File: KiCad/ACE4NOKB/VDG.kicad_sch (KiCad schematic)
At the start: 39 parts, among them Q1 2N3904, Q100 2N3904, X1 CRYSTALHC49U-V 6.5MHz

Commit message: Fix mistake with ROM Select.
Signed-off-by: John Bradley <flypie@rocketmail.com>
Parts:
- removed C1: 30p, Capacitor_THT:C_Disc_D3.8mm_W2.6mm_P2.50mm, symbol Device:C_Small
- removed C2: 100p, Capacitor_THT:C_Disc_D5.0mm_W2.5mm_P5.00mm, symbol Device:C_Small
- removed D100: BAT54W,115, Package_TO_SOT_SMD:SOT-323_SC-70, symbol Diode:BAT54W
- removed D11: 1N4148, Diode_THT:D_DO-35_SOD27_P2.54mm_Vertical_AnodeUp, symbol Diode:1N4148
- removed IC? (x2): 74ACT16825DL, SOP64P1035X279-56N, symbol ExtraSymbols:74ACT16825DL
- removed JCOMPOSITE-OUT1: COMPOSITE-OUT1, Connector_PinHeader_2.54mm:PinHeader_1x02_P2.54mm_Vertical, symbol Connector_Generic:Conn_01x02
- removed Q1, Q100: 2N3904, Package_TO_SOT_THT:TO-92_Inline, symbol Transistor_BJT:2N3904
- removed R1: 4k7, Resistor_THT:R_Axial_DIN0204_L3.6mm_D1.6mm_P1.90mm_Vertical, symbol Device:R
- removed R11, R16: 1K5, Resistor_THT:R_Axial_DIN0204_L3.6mm_D1.6mm_P1.90mm_Vertical, symbol Device:R
- removed R17: 100, Resistor_THT:R_Axial_DIN0204_L3.6mm_D1.6mm_P1.90mm_Vertical, symbol Device:R
- removed R2: 47k, Resistor_THT:R_Axial_DIN0204_L3.6mm_D1.6mm_P1.90mm_Vertical, symbol Device:R
- removed R404, R406, R407: 270, Resistor_THT:R_Axial_DIN0204_L3.6mm_D1.6mm_P1.90mm_Vertical, symbol Device:R
- removed R416, R417: 75k, Resistor_THT:R_Axial_DIN0204_L3.6mm_D1.6mm_P1.90mm_Vertical, symbol Device:R
- removed R418, R419, R420, R422, R? (x2): 1k0, Resistor_THT:R_Axial_DIN0204_L3.6mm_D1.6mm_P1.90mm_Vertical, symbol Device:R
- removed R421: 10k, Resistor_THT:R_Axial_DIN0204_L3.6mm_D1.6mm_P1.90mm_Vertical, symbol Device:R
- removed RV1: 100, ExtraFootprints:3362H1103LF, symbol Device:R_Potentiometer_Trim
- removed X1: CRYSTALHC49U-V 6.5MHz, Crystal:Crystal_HC49-U_Vertical, symbol Device:Crystal
- removed Z19: 74AHCT00, Package_DIP:DIP-14_W7.62mm_Socket, symbol 74xx:74HCT00
- removed Z23: 74AHCT1G86GW,125, ExtraFootprints:TSSOP-5, symbol ExtraSymbols:74AHC1G86GW,125
- removed Z25: 74AHCT02, Package_DIP:DIP-14_W7.62mm_Socket, symbol 74xx:74HCT02
- removed Z28: 74HCT166, Package_DIP:DIP-16_W7.62mm_Socket, symbol 74xx:74LS166
- removed Z306: 74AHCT04, Package_DIP:DIP-14_W7.62mm_Socket, symbol 74xx:74LS04
- removed Z7-8: IDT71321, ExtraFootprints:PLCC-52, symbol ExtraSymbols:IDT71321-421-52PIN-PLCC
- added COMP1: PJRAN1X1U03, ExtraFootprints:PJRAN1X1U01X, symbol ExtraSymbols:PJRAN1X1U03AUX
- added D1: 1N4148, Diode_THT:D_DO-35_SOD27_P2.54mm_Vertical_AnodeUp, symbol Diode:1N4148
- added Q101: 2N3904, Package_TO_SOT_THT:TO-92_Inline, symbol Transistor_BJT:2N3904
- added R100: 100, Resistor_THT:R_Axial_DIN0204_L3.6mm_D1.6mm_P1.90mm_Vertical, symbol Device:R
- added R134, R135, R21, R22, R400, R401, R402: 1K, Resistor_THT:R_Axial_DIN0204_L3.6mm_D1.6mm_P1.90mm_Vertical, symbol Device:R
- added R136, R403: 10K, Resistor_THT:R_Axial_DIN0204_L3.6mm_D1.6mm_P1.90mm_Vertical, symbol Device:R
- added R3, R4: 1K5, Resistor_THT:R_Axial_DIN0204_L3.6mm_D1.6mm_P1.90mm_Vertical, symbol Device:R
- added RN2, RN3: 1k, Package_DIP:DIP-16_W7.62mm, symbol Device:R_Pack08
- added RV101: 100, Potentiometer_THT:Potentiometer_Bourns_3296W_Vertical, symbol Device:R_Potentiometer_Trim
- added Z18: 74LS125, Package_DIP:DIP-14_W7.62mm, symbol 74xx-FIX:74LS125
- added Z19: SN74AHCT00N, Package_DIP:DIP-14_W7.62mm, symbol 74xx:74LS00
- added unit 1 of Z20
- added Z21: SN74ACT11N, Package_DIP:DIP-14_W7.62mm, symbol 74xx:74LS11
- added Z23: SN74AHCT86N, Package_DIP:DIP-14_W7.62mm, symbol 74xx:74LS86
- added Z25: SN74AHCT02, Package_DIP:DIP-14_W7.62mm, symbol 74xx:74LS02
- added Z28: SN74ALS166N, Package_DIP:DIP-16_W7.62mm, symbol 74xx-FIX:74LS166
- added Z7-8: 6116P, Package_DIP:DIP-24_W7.62mm, symbol ExtraSymbols:6116P
- R405: value 270 -> 1K; Manufacturer_Part_Number CCF07270RGKE36 -> MBA02040C4708FRP00
- Z20: value 74AHCT08 -> SN74AHCT08N; footprint Package_DIP:DIP-14_W7.62mm_Socket -> Package_DIP:DIP-14_W7.62mm; Manufacturer_Name Texas Instruments -> (none); Manufacturer_Part_Number SN74AHCT08N -> (none)
- Z22: value 74HCT11 -> SN74ACT11N; footprint Package_DIP:DIP-14_W7.62mm_Socket -> Package_DIP:DIP-14_W7.62mm; Manufacturer_Name Texas Instruments -> (none); Manufacturer_Part_Number CD74HCT11M -> (none)
- Z27: value 74AHCT74 -> SN74AHCT74N; footprint Package_DIP:DIP-14_W7.62mm_Socket -> Package_DIP:DIP-14_W7.62mm; Manufacturer_Name Texas Instruments -> (none); Manufacturer_Part_Number SN74AHCT74N -> (none)
- Z5-6: value IDT71321 -> 7132LA100PDG; footprint ExtraFootprints:PLCC-52 -> ExtraFootprints:PLCC-52_THT-Socket
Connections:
- net A0: now also RN3.1 (R1.1)
- net A1: now also RN3.2 (R2.1)
- net A2: now also RN3.3 (R3.1)
- net A3: now also RN3.4 (R4.1)
- net A4: now also RN3.5 (R5.1)
- net A5: now also RN3.6 (R6.1)
- net A6: now also RN3.7 (R7.1)
- net A7: now also RN3.8 (R8.1)
- net A8: now also R21.1
- net A9: now also R22.1
- net GND: now also R405.1, COMP1.1 (SLEEVE), R100.2, R134.1, R135.1, R400.1, R401.1, R402.1, Z28.8 (GND), Z7-8.12 (GND)
- net SCREENX2: now also Z21.9, Z25.8
- net SCREENX4: now also Z21.10, Z25.9
- net SCREENY0: now also Z21.1
- net SCREENY1: now also Z21.2
- net SCREENY2: now also Z21.13
- net SCREENY3: now also Z19.2, Z21.3
- net SCREENY4: now also Z19.1, Z21.4
- net VCC: now also Q101.3 (C), R136.1, R4.1, R403.1, Z28.16 (VCC), Z7-8.24 (VCC); no longer R405.2
- net VIDEO: now also Q101.1 (E), R100.1, RV101.1
- net at Z27.9 (Q): now also Z23.12
- net at Z20.4: now also Z19.3
- net ~{IN_VBI_OR_HBI}: now reaches Z20.12, Z20.6
- net ~{IN_VBI_OR_HBI}: now also Z19.4
- net at Z20.5: now also Z25.1
- net VA9: now reaches Z5-6.33 (I/O6_{R})
- net VA9: now also R22.2, Z7-8.22 (A9)
- net VA8: now reaches Z5-6.32 (I/O5_{R})
- net VA8: now also R21.2, Z7-8.23 (A8)
- net VA7: now reaches Z5-6.31 (I/O4_{R})
- net VA7: now also RN3.9 (R8.2), Z7-8.1 (A7)
- net VA6: now reaches Z5-6.30 (I/O3_{R})
- net VA6: now also RN3.10 (R7.2), Z7-8.2 (A6)
- net VA5: now reaches Z5-6.29 (I/O2_{R})
- net VA5: now also RN3.11 (R6.2), Z7-8.3 (A5)
- net VA4: now reaches Z5-6.28 (I/O1_{R})
- net VA4: now also RN3.12 (R5.2), Z7-8.4 (A4)
- net VA3: now reaches Z5-6.27 (I/O0_{R})
- net VA3: now also RN3.13 (R4.2), Z7-8.5 (A3)
- net at Z5-6.3 (~{BUSY}_{L}): no longer R405.1
- net at Z5-6.47 (A10_{R}): now also R401.2
- net at Z5-6.5 (A10_{L}): now also R400.2
- net at Z5-6.50 (R/~{W}_{R}): now also R403.2
- net H_SYNC_PULSE: now reaches Z22.12
- net H_SYNC_PULSE: now also Z25.5
- net at Z22.2: now also Z25.10
- net CNT0 renamed FONTCHARX0
- net CNT1 renamed FONTCHARX1
- net CNT2 renamed FONTCHARX2
- net DA0 renamed D0
- net D0: now also RN2.1 (R1.1)
- net DA1 renamed D1
- net D1: now also RN2.2 (R2.1)
- net DA2 renamed D2
- net D2: now also RN2.3 (R3.1)
- net DA3 renamed D3
- net D3: now also RN2.4 (R4.1)
- net DA4 renamed D4
- net D4: now also RN2.5 (R5.1)
- net DA5 renamed D5
- net D5: now also RN2.6 (R6.1)
- net DA6 renamed D6
- net D6: now also RN2.7 (R7.1)
- net DA7 renamed D7
- net D7: now also RN2.8 (R8.1)
- net EOL renamed SCREENX5
- net SCREENX5: now also Z21.11, Z25.3
- net SH~{LD}: no longer names the net of Z5-6.51 (~{CE}_{R})
- net SH~{LD}: now also R402.2; no longer Z5-6.46 (~{OER})
- net VIDEN renamed LOAD_SHIFT_REG
- net LOAD_SHIFT_REG: now also Z19.5
- net ~{CPUVIDEORAM} renamed ~{CPU2VRAM}
- net ~{VIDEOCLK} renamed VDGCLK
- net VDGCLK: now also Z28.7 (CLK)
- net ~{WAIT}: no longer names the net of Z5-6.49 (~{BUSY}_{R})
- new net: R134.2, Z28.1 (SER)
- new net: R135.2, Z28.6 (CLK_INH)
- new net: R136.2, Z28.9 (~{CLR})
- new net: R3.2, Z23.11
- new net: Z20.1, Z21.12, Z21.5
- new net: R405.2, Z7-8.19 (A10)
- new net: COMP1.2 (TIP), RV101.2
- new net FONTCHARY0: Z18.5
- new net FONTCHARY1: Z18.9
- new net FONTCHARY2: Z18.12
- new net PIXEL: Z23.13, Z28.13 (Qh)
- new net RAWVIDEO: D1.2 (A), Q101.2 (B), R3.1, R4.2
- new net SCREENY5: Z20.2, Z25.2
- new net SHIFT/~{LOAD}: Z19.6, Z28.15 (SH/~{LD}), Z5-6.46 (~{OE}_{R})
- new net VA0: RN3.16 (R1.2), Z18.6, Z7-8.8 (A0)
- new net VA1: RN3.15 (R2.2), Z18.8, Z7-8.7 (A1)
- new net VA2: RN3.14 (R3.2), Z18.11, Z7-8.6 (A2)
- new net VD0: RN2.16 (R1.2), Z28.2 (A), Z7-8.9 (D0)
- new net VD1: RN2.15 (R2.2), Z28.3 (B), Z7-8.10 (D1)
- new net VD2: RN2.14 (R3.2), Z28.4 (C), Z7-8.11 (D2)
- new net VD3: RN2.13 (R4.2), Z28.5 (D), Z7-8.13 (D3)
- new net VD4: RN2.12 (R5.2), Z28.10 (E), Z7-8.14 (D4)
- new net VD5: RN2.11 (R6.2), Z28.11 (F), Z7-8.15 (D5)
- new net VD6: RN2.10 (R7.2), Z28.12 (G), Z7-8.16 (D6)
- new net VD7: RN2.9 (R8.2), Z28.14 (H), Z7-8.17 (D7)
- new net V_SYNC_PULSE(50Hz): Z21.6, Z25.6
- new net XRESET: Z21.8
- new net YRESET: Z20.3
- new net ~{CPUVDGRD}: Z18.10, Z18.13, Z18.4, Z7-8.20 (~{OE})
- new net ~{CPUVDGWR}: Z7-8.21 (~{WE})
- new net ~{FONTRAMCS}: Z7-8.18 (~{CS})
- new net ~{SYNC_PULSE}: D1.1 (K), Z25.4
- no-connect marks 6 -> 7
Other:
- removed sheet Cascade4040
- note added: "END_OF_PIX_V"
- title: ACE4NOKB -> JupiterAce Z80 plus KIO and new memory format.

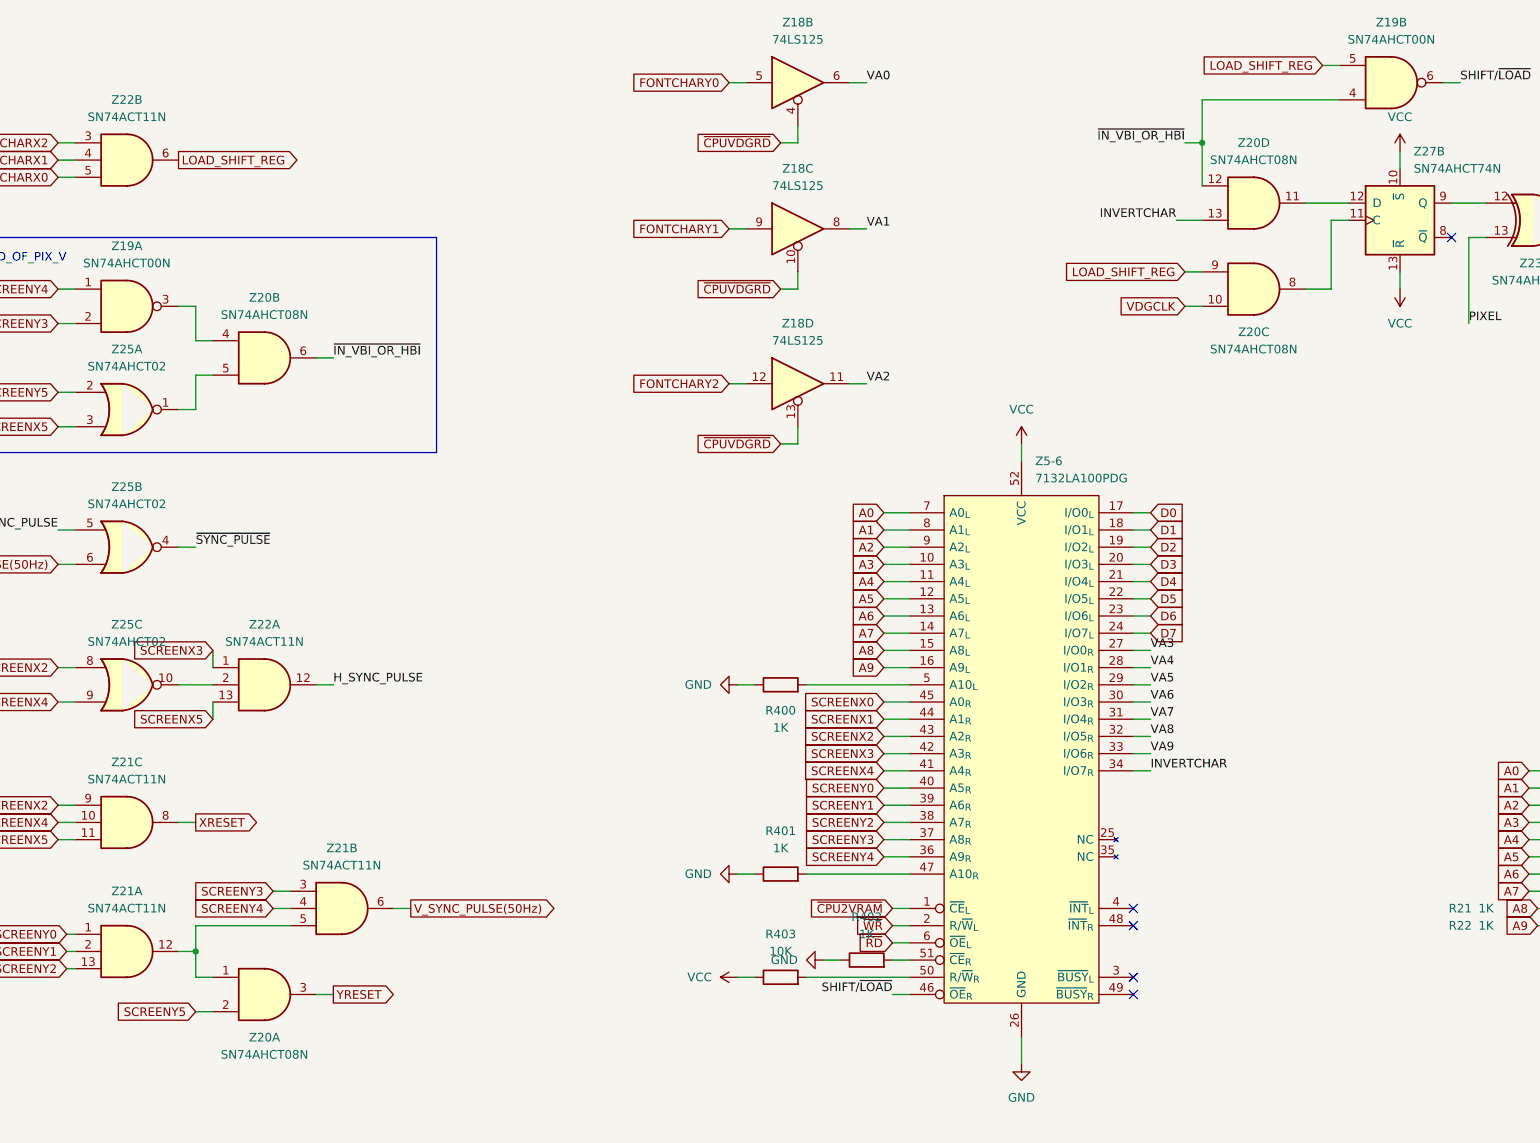
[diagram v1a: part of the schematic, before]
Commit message: Update to last expermintal version. Uses clock sythsiser and can be switched between full ACE compatible and inhanced IO. Should be able to switch between multiple ROM images tosred on the same chip.
Signed-off-by: John Bradley <flypie@rocketmail.com>
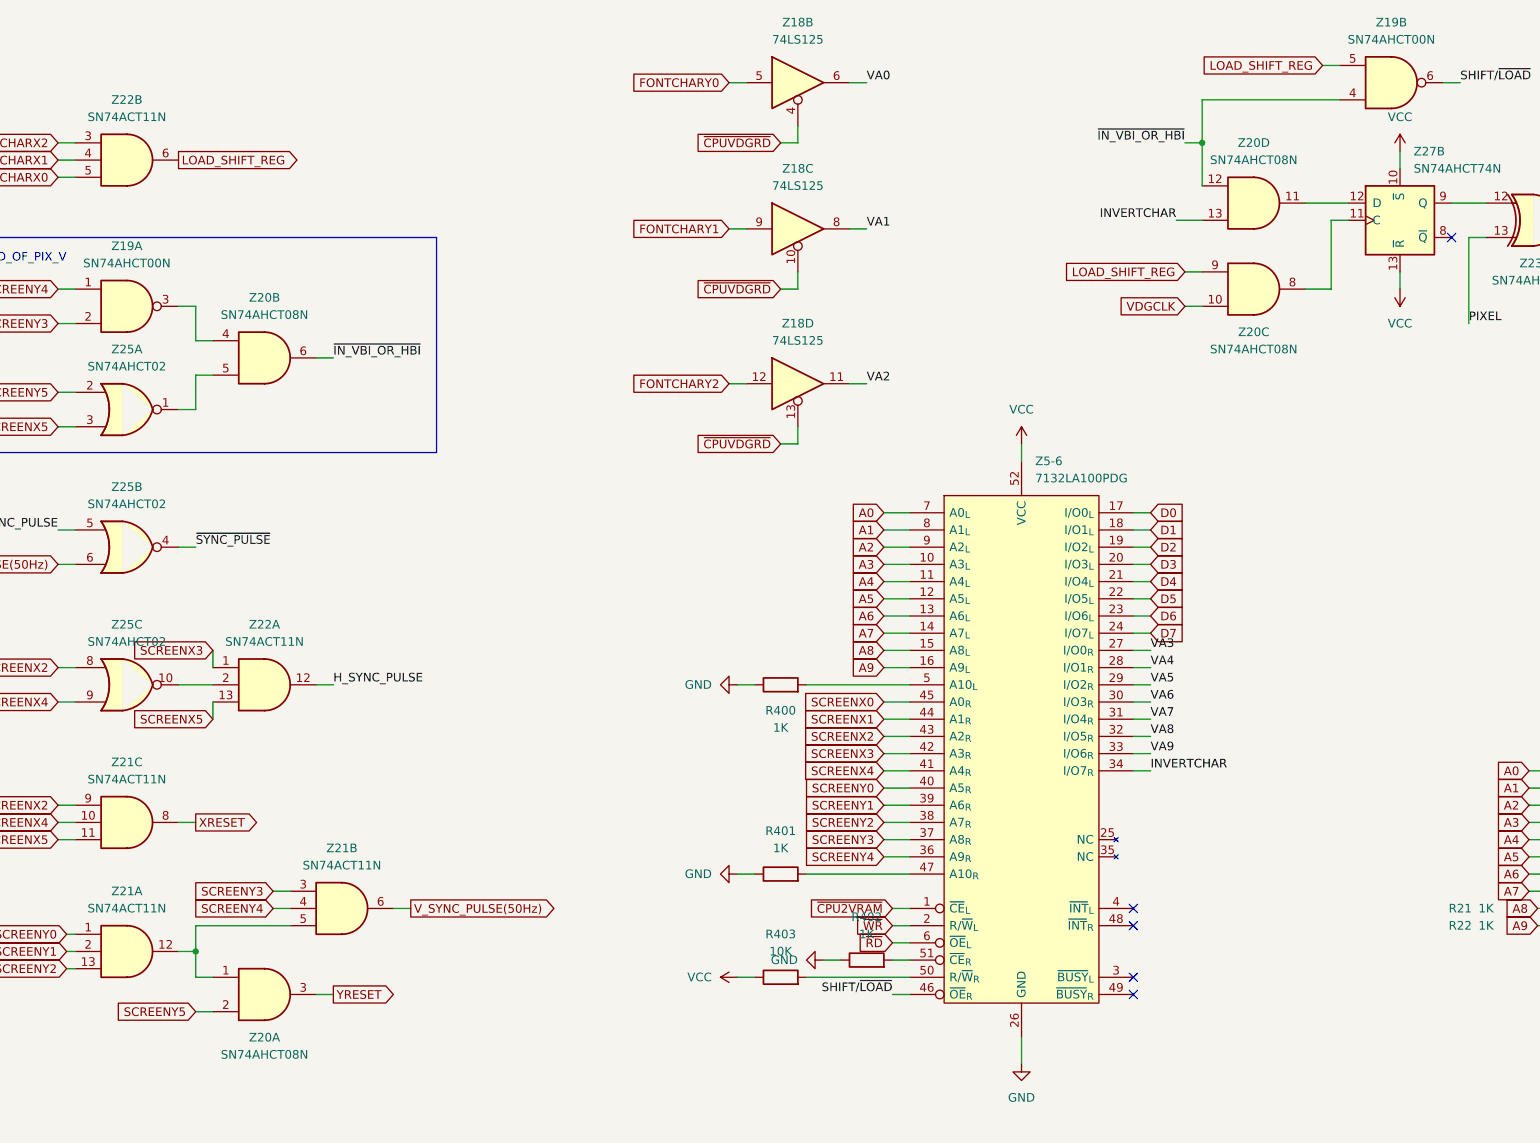
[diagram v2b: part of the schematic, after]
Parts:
- COMP1: Field4 (none) -> Conn Rca Jack Mono 3.2mm r/a; Field5 (none) -> None; Field6 (none) -> PJRAN1X1U03AUX; Field7 (none) -> Unavailable; Field8 (none) -> Switchcraft Inc.
- R134, R135: Manufacturer_Name Vishay -> (none); Manufacturer_Part_Number MBA02040C1202FRP00 -> (none)
- R136: Manufacturer_Name Vishay -> (none); Manufacturer_Part_Number MBA02040C1002FRP00 -> (none)
- R400, R401, R402, R403, R405: Manufacturer_Name Vishay -> (none); Manufacturer_Part_Number MBA02040C4708FRP00 -> (none)
- Z25: Manufacturer_Name Texas Instruments -> (none); Manufacturer_Part_Number SN74AHCT02N -> (none)
- Z28: Manufacturer_Name Texas Instruments -> (none); Manufacturer_Part_Number SN74ALS166N -> (none)

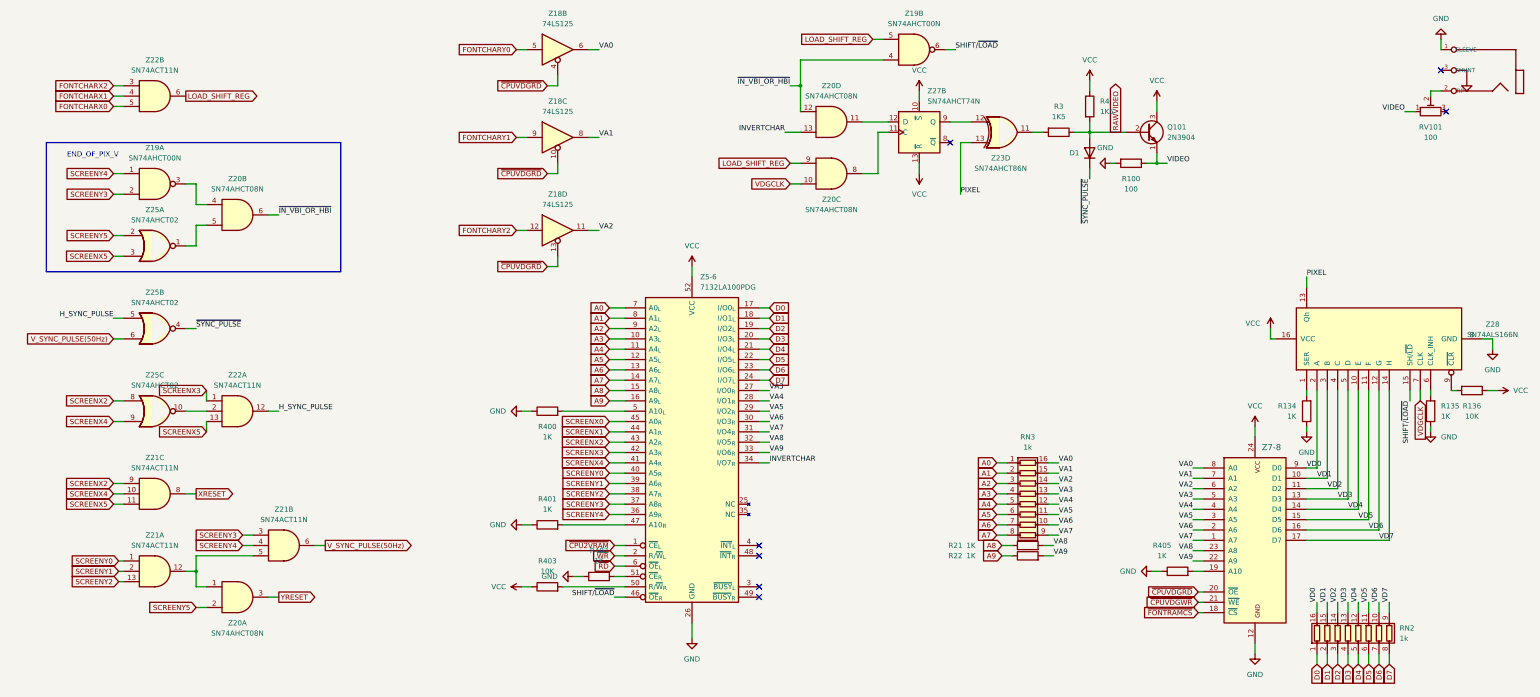
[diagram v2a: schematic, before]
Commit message: Version with KIO replaced with Z84C15 and Video and Character RAM as MultiPorted.
Signed-off-by: John Bradley <flypie@rocketmail.com>
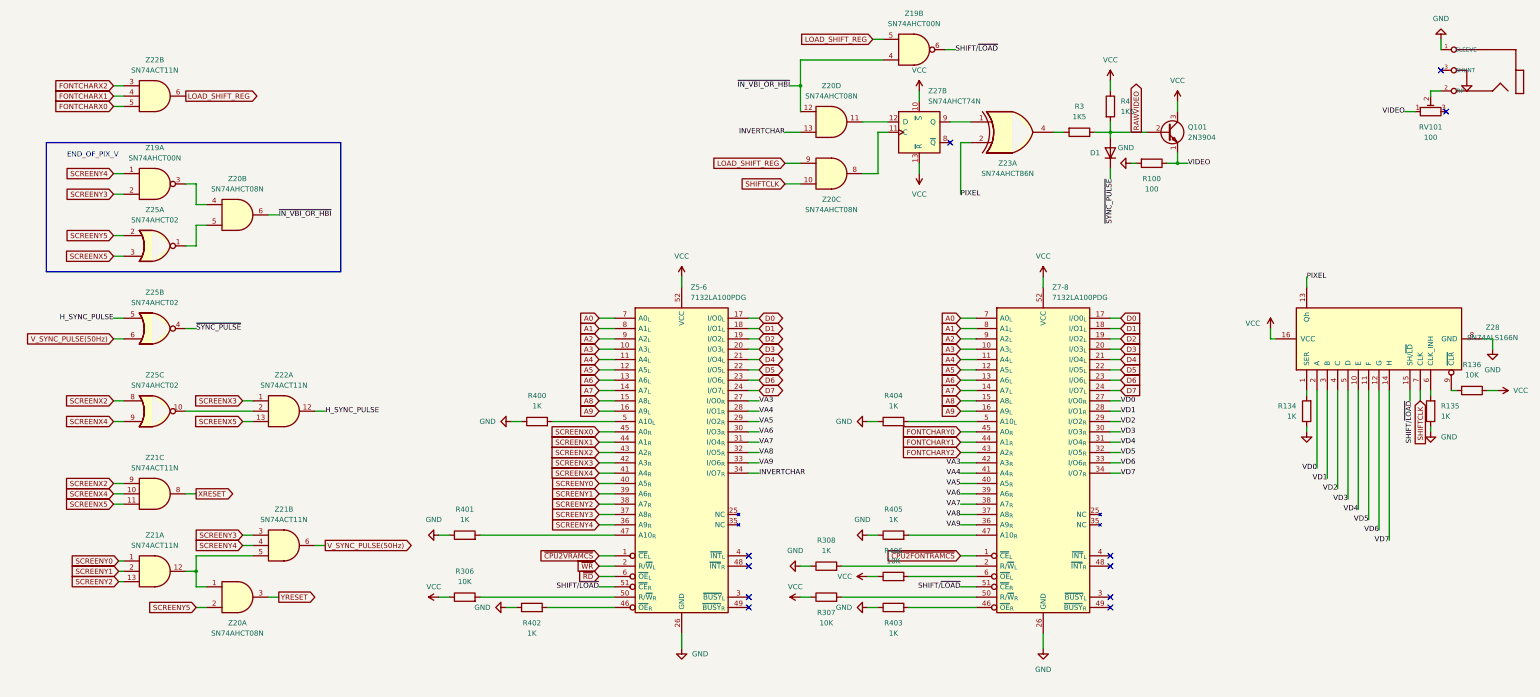
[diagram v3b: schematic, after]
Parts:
- removed R21, R22: 1K, Resistor_THT:R_Axial_DIN0204_L3.6mm_D1.6mm_P1.90mm_Vertical, symbol Device:R
- removed RN2, RN3: 1k, Package_DIP:DIP-16_W7.62mm, symbol Device:R_Pack08
- removed Z18: 74LS125, Package_DIP:DIP-14_W7.62mm, symbol 74xx-FIX:74LS125
- removed Z7-8: 6116P, Package_DIP:DIP-24_W7.62mm, symbol ExtraSymbols:6116P
- added R306, R307, R406: 10K, Resistor_THT:R_Axial_DIN0204_L3.6mm_D1.6mm_P1.90mm_Vertical, symbol Device:R
- added R308, R404: 1K, Resistor_THT:R_Axial_DIN0204_L3.6mm_D1.6mm_P1.90mm_Vertical, symbol Device:R
- added Z7-8: 7132LA100PDG, ExtraFootprints:PLCC-52_THT-Socket, symbol ExtraSymbols:IDT71321-421-52PIN-PLCC
- Q101: footprint Package_TO_SOT_THT:TO-92_Inline -> Package_TO_SOT_THT:TO-92_Inline_Wide
- R403: value 10K -> 1K
- Z23: footprint Package_DIP:DIP-14_W7.62mm -> Package_TO_SOT_SMD:SOT-23-5_HandSoldering; symbol 74xx:74LS86 -> 74xGxx:74AHCT1G86
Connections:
- net A0: now also Z7-8.7 (A0_{L})
- net A1: now also Z7-8.8 (A1_{L})
- net A2: now also Z7-8.9 (A2_{L})
- net A3: now also Z7-8.10 (A3_{L})
- net A4: now also Z7-8.11 (A4_{L})
- net A5: now also Z7-8.12 (A5_{L})
- net A6: now also Z7-8.13 (A6_{L})
- net A7: now also Z7-8.14 (A7_{L})
- net A8: now also Z7-8.15 (A8_{L})
- net A9: now also Z7-8.16 (A9_{L})
- net D0: now also Z7-8.17 (I/O0_{L})
- net D1: now also Z7-8.18 (I/O1_{L})
- net D2: now also Z7-8.19 (I/O2_{L})
- net D3: now also Z7-8.20 (I/O3_{L})
- net D4: now also Z7-8.21 (I/O4_{L})
- net D5: now also Z7-8.22 (I/O5_{L})
- net D6: now also Z7-8.23 (I/O6_{L})
- net D7: now also Z7-8.24 (I/O7_{L})
- net FONTCHARY0: now also Z7-8.45 (A0_{R})
- net FONTCHARY1: now also Z7-8.44 (A1_{R})
- net FONTCHARY2: now also Z7-8.43 (A2_{R})
- net GND: now also R403.1, R308.1, R404.1, Z7-8.26 (GND)
- net PIXEL: now also Z23.2; no longer Z23.13
- net SHIFT/~{LOAD}: now also Z5-6.51 (~{CE}_{R}), Z7-8.51 (~{CE}_{R}); no longer Z5-6.46 (~{OE}_{R})
- net VA3: now also Z7-8.42 (A3_{R})
- net VA4: now also Z7-8.41 (A4_{R})
- net VA5: now also Z7-8.40 (A5_{R})
- net VA6: now also Z7-8.39 (A6_{R})
- net VA7: now also Z7-8.38 (A7_{R})
- net VA8: now also Z7-8.37 (A8_{R})
- net VA9: now also Z7-8.36 (A9_{R})
- net VCC: now also R306.1, R307.1, R406.1, Z7-8.52 (VCC); no longer R403.1
- net VD0: now also Z7-8.27 (I/O0_{R})
- net VD1: now also Z7-8.28 (I/O1_{R})
- net VD2: now also Z7-8.29 (I/O2_{R})
- net VD3: now also Z7-8.30 (I/O3_{R})
- net VD4: now also Z7-8.31 (I/O4_{R})
- net VD5: now also Z7-8.32 (I/O5_{R})
- net VD6: now also Z7-8.33 (I/O6_{R})
- net VD7: now also Z7-8.34 (I/O7_{R})
- net at R3.2: now also Z23.4; no longer Z23.11
- net at R403.2: now also Z7-8.46 (~{OE}_{R}); no longer Z5-6.50 (R/~{W}_{R})
- net at R402.2: now also Z5-6.46 (~{OE}_{R}); no longer Z5-6.51 (~{CE}_{R})
- net at R405.2: now also Z7-8.47 (A10_{R})
- net at Z27.9 (Q): now also Z23.1; no longer Z23.12
- net VDGCLK renamed SHIFTCLK
- net ~{CPU2VRAM} renamed ~{CPU2VRAMCS}
- new net: R307.2, Z7-8.50 (R/~{W}_{R})
- new net: R308.2, Z7-8.2 (R/~{W}_{L})
- new net: R404.2, Z7-8.5 (A10_{L})
- new net: R406.2, Z7-8.6 (~{OE}_{L})
- new net: R306.2, Z5-6.50 (R/~{W}_{R})
- new net ~{CPU2FONTRAMCS}: Z7-8.1 (~{CE}_{L})
- no-connect marks 7 -> 11
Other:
- moved on the sheet: D1, Q101, R100, R3, R4, R400, R401, R402, R405, Z22A, Z5-6
